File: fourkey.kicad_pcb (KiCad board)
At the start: 2 copper layers, 85.3 x 77.7 mm, 23 parts, among them K1 KEYSW, K2 KEYSW, K3 KEYSW, K4 KEYSW, SW1 SW_PUSH, U1 ProMicro

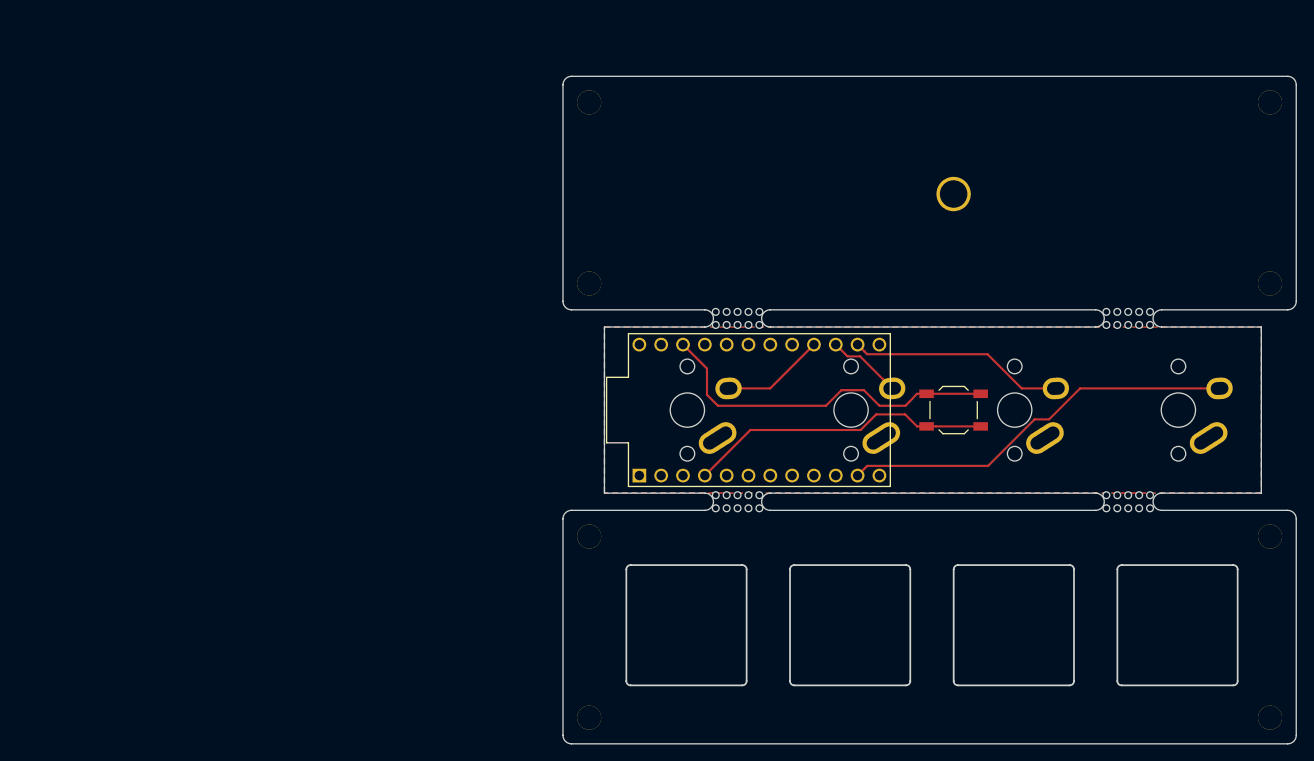
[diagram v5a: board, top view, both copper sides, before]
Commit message: fine tune screw/switch hole placement
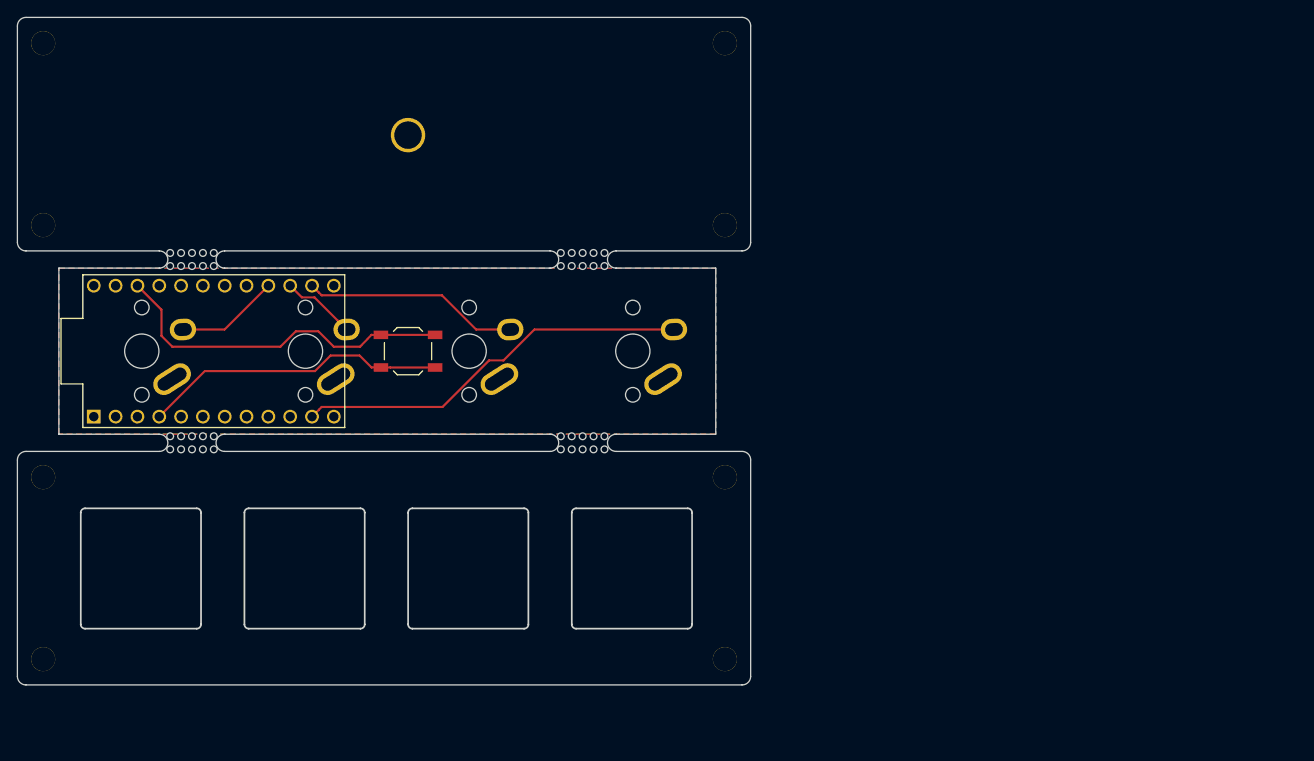
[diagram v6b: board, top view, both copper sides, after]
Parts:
- removed the HOLE_M2.6 at (130.0, 122.2)
- removed the HOLE_M2.6 at (209.3, 122.2)
- removed the HOLE_M2.6 at (130.0, 101.1)
- removed the HOLE_M2.6 at (209.3, 101.1)
- removed the HOLE_M2.6 at (130.0, 71.6)
- removed the HOLE_M2.6 at (130.0, 50.5)
- removed the HOLE_M2.6 at (209.3, 50.5)
- removed the HOLE_M2.6 at (209.3, 71.6)
- removed the REF** at (147.3, 98.0)
- removed the REF** at (192.8, 98.0)
- removed the REF** at (192.8, 74.7)
- removed the REF** at (147.3, 74.7)
- removed the REF** at (147.3, 76.7)
- removed the REF** at (192.8, 76.7)
- removed the REF** at (192.8, 96.0)
- removed the REF** at (147.3, 96.0)
- added HOLE_M2.6: VAL**, keyboard_parts:HOLE_M2.6, B.Cu at (66.5, 115.3)
- added HOLE_M2.6: VAL**, keyboard_parts:HOLE_M2.6, B.Cu at (145.8, 115.3)
- added HOLE_M2.6: VAL**, keyboard_parts:HOLE_M2.6, B.Cu at (66.5, 94.2)
- added HOLE_M2.6: VAL**, keyboard_parts:HOLE_M2.6, B.Cu at (145.8, 94.2)
- added HOLE_M2.6: VAL**, keyboard_parts:HOLE_M2.6, F.Cu at (66.5, 64.8)
- added HOLE_M2.6: VAL**, keyboard_parts:HOLE_M2.6, F.Cu at (66.5, 43.7)
- added HOLE_M2.6: VAL**, keyboard_parts:HOLE_M2.6, F.Cu at (145.8, 43.7)
- added HOLE_M2.6: VAL**, keyboard_parts:HOLE_M2.6, F.Cu at (145.8, 64.8)
- added REF**: breakaway-mousebites, Keebio-Parts:breakaway-mousebites, F.Cu at (83.8, 91.2)
- added REF**: breakaway-mousebites, Keebio-Parts:breakaway-mousebites, F.Cu at (129.3, 91.2)
- added REF**: breakaway-mousebites, Keebio-Parts:breakaway-mousebites, F.Cu at (129.3, 67.8)
- added REF**: breakaway-mousebites, Keebio-Parts:breakaway-mousebites, F.Cu at (83.8, 67.8)
- added REF**: breakaway-mousebites, Keebio-Parts:breakaway-mousebites, F.Cu at (83.8, 69.8)
- added REF**: breakaway-mousebites, Keebio-Parts:breakaway-mousebites, F.Cu at (129.3, 69.8)
- added REF**: breakaway-mousebites, Keebio-Parts:breakaway-mousebites, F.Cu at (129.3, 89.2)
- added REF**: breakaway-mousebites, Keebio-Parts:breakaway-mousebites, F.Cu at (83.8, 89.2)
- moved K1 63.9 mm to (78.0, 79.5)
- moved SW1 63.9 mm to (109.0, 79.5)
- moved U1 63.9 mm to (86.4, 79.5)
- moved HOLE_M3 63.9 mm to (109.0, 54.4)
- moved K3 63.9 mm to (116.1, 79.5)
- moved K4 63.9 mm to (135.1, 79.5)
- moved K2 63.9 mm to (97.0, 79.5)
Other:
- outline, holes or cut-outs redrawn

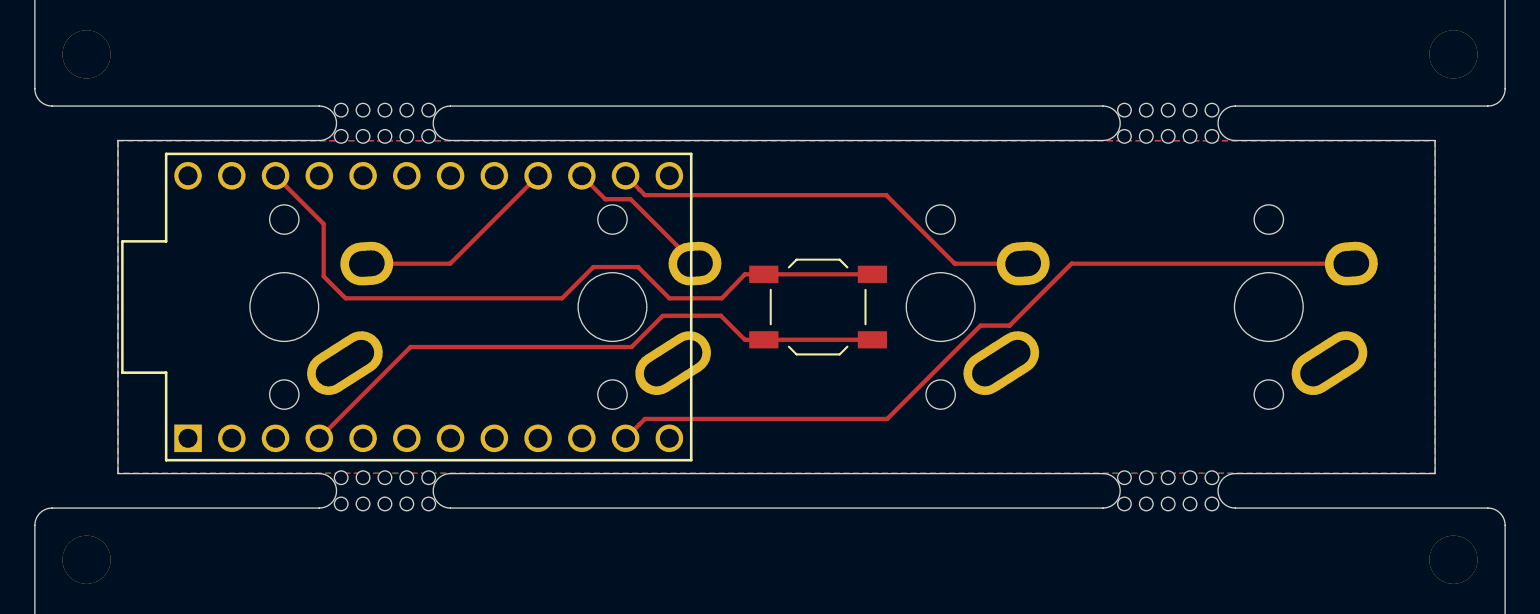
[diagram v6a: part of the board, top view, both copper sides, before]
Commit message: symetrify breakaway tabs
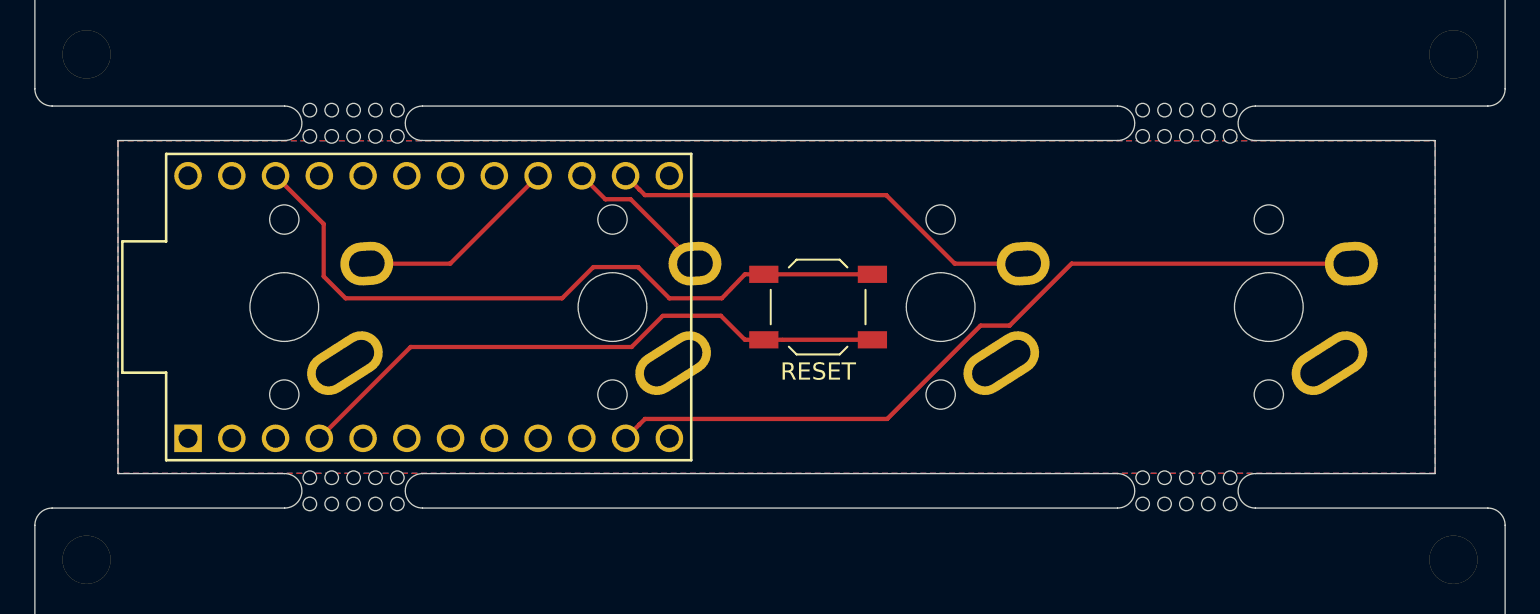
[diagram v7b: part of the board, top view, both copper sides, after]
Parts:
- removed the REF** at (83.8, 91.2)
- removed the REF** at (129.3, 91.2)
- removed the REF** at (83.8, 89.2)
- added REF**: breakaway-mousebites, Keebio-Parts:breakaway-mousebites, F.Cu at (82.0, 91.2)
- added REF**: breakaway-mousebites, Keebio-Parts:breakaway-mousebites, F.Cu at (130.3, 91.2)
- added REF**: breakaway-mousebites, Keebio-Parts:breakaway-mousebites, F.Cu at (82.0, 89.2)
- SW1: value SW_PUSH -> RESET
- moved REF** 1.82 mm to (82.0, 67.8)
- moved REF** 1.82 mm to (82.0, 69.8)
- moved REF** 1.06 mm to (130.3, 67.8)
- moved REF** 1.06 mm to (130.3, 69.8)
- moved REF** 1.06 mm to (130.3, 89.2)
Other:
- outline, holes or cut-outs redrawn
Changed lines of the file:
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@@
   )
   (module Keebio-Parts:breakaway-mousebites (layer F.Cu)
-    (at 83.82 91.186)
+    (at 82 91.186)
     (fp_text reference REF** (at 0 -3.048) (layer Dwgs.User) hide
       (effects (font (size 1 1) (thickness 0.15)))
@@
   )
   (module Keebio-Parts:breakaway-mousebites (layer F.Cu)
-    (at 129.286 91.186)
+    (at 130.344 91.186)
     (fp_text reference REF** (at 0 -3.048) (layer Dwgs.User) hide
       (effects (font (size 1 1) (thickness 0.15)))
@@
   )
   (module Keebio-Parts:breakaway-mousebites (layer F.Cu)
-    (at 129.286 67.818 180)
+    (at 130.344 67.818 180)
     (fp_text reference REF** (at 0 -3.048) (layer Dwgs.User) hide
       (effects (font (size 1 1) (thickness 0.15)))
@@
   )
   (module Keebio-Parts:breakaway-mousebites (layer F.Cu)
-    (at 83.82 67.818 180)
+    (at 82 67.818 180)
     (fp_text reference REF** (at 0 -3.048) (layer Dwgs.User) hide
       (effects (font (size 1 1) (thickness 0.15)))
@@
   )
   (module Keebio-Parts:breakaway-mousebites (layer F.Cu)
-    (at 83.82 69.85)
+    (at 82 69.85)
     (fp_text reference REF** (at 0 -3.048) (layer Dwgs.User) hide
       (effects (font (size 1 1) (thickness 0.15)))
@@
   )
   (module Keebio-Parts:breakaway-mousebites (layer F.Cu)
-    (at 129.286 69.85)
+    (at 130.344 69.85)
     (fp_text reference REF** (at 0 -3.048) (layer Dwgs.User) hide
       (effects (font (size 1 1) (thickness 0.15)))
@@
   )
   (module Keebio-Parts:breakaway-mousebites (layer F.Cu)
-    (at 129.286 89.154 180)
+    (at 130.344 89.154 180)
     (fp_text reference REF** (at 0 -3.048) (layer Dwgs.User) hide
       (effects (font (size 1 1) (thickness 0.15)))
@@
   )
   (module Keebio-Parts:breakaway-mousebites (layer F.Cu)
-    (at 83.82 89.154 180)
+    (at 82 89.154 180)
     (fp_text reference REF** (at 0 -3.048) (layer Dwgs.User) hide
       (effects (font (size 1 1) (thickness 0.15)))
@@
       (effects (font (size 1 1) (thickness 0.15)))
     )
-    (fp_text value SW_PUSH (at 0 3.75) (layer F.Fab)
+    (fp_text value RESET (at 0 3.75) (layer F.SilkS)
       (effects (font (size 1 1) (thickness 0.15)))
     )
@@
   (gr_arc (start 64.5 117.348) (end 63.5 117.348) (angle -90) (layer Edge.Cuts) (width 0.05))
   (gr_arc (start 64.5 92.17) (end 64.5 91.17) (angle -90) (layer Edge.Cuts) (width 0.05))
-  (gr_arc (start 87.622 68.834) (end 87.622 67.834) (angle -180) (layer Edge.Cuts) (width 0.05))
-  (gr_arc (start 80.01 68.834) (end 80.01 67.834) (angle 180) (layer Edge.Cuts) (width 0.05))
-  (gr_arc (start 133.18 68.834) (end 133.18 67.834) (angle -180) (layer Edge.Cuts) (width 0.05))
-  (gr_arc (start 125.5 68.834) (end 125.5 67.834) (angle 180) (layer Edge.Cuts) (width 0.05))
-  (gr_arc (start 133.18 90.17) (end 133.18 89.17) (angle -180) (layer Edge.Cuts) (width 0.05))
-  (gr_arc (start 125.5 90.17) (end 125.5 89.17) (angle 180) (layer Edge.Cuts) (width 0.05))
-  (gr_arc (start 87.622 90.17) (end 87.622 89.17) (angle -180) (layer Edge.Cuts) (width 0.05))
-  (gr_arc (start 80.01 90.17) (end 80.01 89.17) (angle 180) (layer Edge.Cuts) (width 0.05))
+  (gr_arc (start 86 68.834) (end 86 67.834) (angle -180) (layer Edge.Cuts) (width 0.05))
+  (gr_arc (start 78 68.834) (end 78 67.834) (angle 180) (layer Edge.Cuts) (width 0.05))
+  (gr_arc (start 134.344 68.834) (end 134.344 67.834) (angle -180) (layer Edge.Cuts) (width 0.05))
+  (gr_arc (start 126.344 68.834) (end 126.344 67.834) (angle 180) (layer Edge.Cuts) (width 0.05))
+  (gr_arc (start 134.344 90.17) (end 134.344 89.17) (angle -180) (layer Edge.Cuts) (width 0.05))
+  (gr_arc (start 126.344 90.17) (end 126.344 89.17) (angle 180) (layer Edge.Cuts) (width 0.05))
+  (gr_arc (start 86 90.17) (end 86 89.17) (angle -180) (layer Edge.Cuts) (width 0.05))
+  (gr_arc (start 78 90.17) (end 78 89.17) (angle 180) (layer Edge.Cuts) (width 0.05))
   (gr_line (start 147.844 118.348) (end 64.5 118.348) (layer Edge.Cuts) (width 0.05))
   (gr_line (start 148.844 92.17) (end 148.844 117.348) (layer Edge.Cuts) (width 0.05))
-  (gr_line (start 64.5 91.17) (end 80.01 91.17) (layer Edge.Cuts) (width 0.05))
+  (gr_line (start 64.5 91.17) (end 78 91.17) (layer Edge.Cuts) (width 0.05))
   (gr_line (start 63.5 92.17) (end 63.5 117.348) (layer Edge.Cuts) (width 0.05))
-  (gr_line (start 133.18 91.17) (end 147.844 91.17) (layer Edge.Cuts) (width 0.05))
-  (gr_line (start 87.622 91.17) (end 125.5 91.17) (layer Edge.Cuts) (width 0.05))
-  (gr_line (start 133.18 89.17) (end 144.78 89.17) (layer Edge.Cuts) (width 0.05))
-  (gr_line (start 87.622 89.17) (end 125.5 89.17) (layer Edge.Cuts) (width 0.05))
-  (gr_line (start 125.5 69.834) (end 87.622 69.834) (layer Edge.Cuts) (width 0.05))
-  (gr_line (start 133.18 67.834) (end 147.844 67.834) (layer Edge.Cuts) (width 0.05))
-  (gr_line (start 80.01 69.834) (end 68.326 69.834) (layer Edge.Cuts) (width 0.05))
-  (gr_line (start 87.622 67.834) (end 125.5 67.834) (layer Edge.Cuts) (width 0.05))
+  (gr_line (start 134.344 91.17) (end 147.844 91.17) (layer Edge.Cuts) (width 0.05))
+  (gr_line (start 86 91.17) (end 126.344 91.17) (layer Edge.Cuts) (width 0.05))
+  (gr_line (start 134.344 89.17) (end 144.78 89.17) (layer Edge.Cuts) (width 0.05))
+  (gr_line (start 86 89.17) (end 126.344 89.17) (layer Edge.Cuts) (width 0.05))
+  (gr_line (start 126.344 69.834) (end 86 69.834) (layer Edge.Cuts) (width 0.05))
+  (gr_line (start 134.344 67.834) (end 147.844 67.834) (layer Edge.Cuts) (width 0.05))
+  (gr_line (start 78 69.834) (end 68.326 69.834) (layer Edge.Cuts) (width 0.05))
+  (gr_line (start 86 67.834) (end 126.344 67.834) (layer Edge.Cuts) (width 0.05))
   (gr_line (start 147.844 40.656) (end 64.5 40.656) (layer Edge.Cuts) (width 0.05))
   (gr_line (start 63.5 41.656) (end 63.5 66.834) (layer Edge.Cuts) (width 0.05))
-  (gr_line (start 64.5 67.834) (end 80.01 67.834) (layer Edge.Cuts) (width 0.05))
+  (gr_line (start 64.5 67.834) (end 78 67.834) (layer Edge.Cuts) (width 0.05))
   (gr_line (start 148.844 66.834) (end 148.844 41.656) (layer Edge.Cuts) (width 0.05))
   (gr_line (start 144.78 89.17) (end 144.78 69.834) (layer Edge.Cuts) (width 0.05))
-  (gr_line (start 68.326 89.17) (end 80.01 89.17) (layer Edge.Cuts) (width 0.05))
+  (gr_line (start 68.326 89.17) (end 78 89.17) (layer Edge.Cuts) (width 0.05))
   (gr_line (start 68.326 69.834) (end 68.326 89.17) (layer Edge.Cuts) (width 0.05))
-  (gr_line (start 144.78 69.834) (end 133.18 69.834) (layer Edge.Cuts) (width 0.05))
+  (gr_line (start 144.78 69.834) (end 134.344 69.834) (layer Edge.Cuts) (width 0.05))
   (segment (start 87.61 76.982) (end 92.71 71.882) (width 0.25) (layer F.Cu) (net 2))
   (segment (start 82.768 76.982) (end 87.61 76.982) (width 0.25) (layer F.Cu) (net 2))
